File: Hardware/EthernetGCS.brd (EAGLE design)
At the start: 72.4 x 46 mm, 80 parts, among them IC1 PIC24FJ64GA002_QFN, IC3 24AA00OT, J2 HR911105A, Q2 25Mhz, U1 MIC5219-3.3V, U3 MIC5219-3.3V, U4 ENC28J60-QFN, U5 MIC5219-3.3V, U7 FT232RL-BASICSSOP, X2 USB-A-H

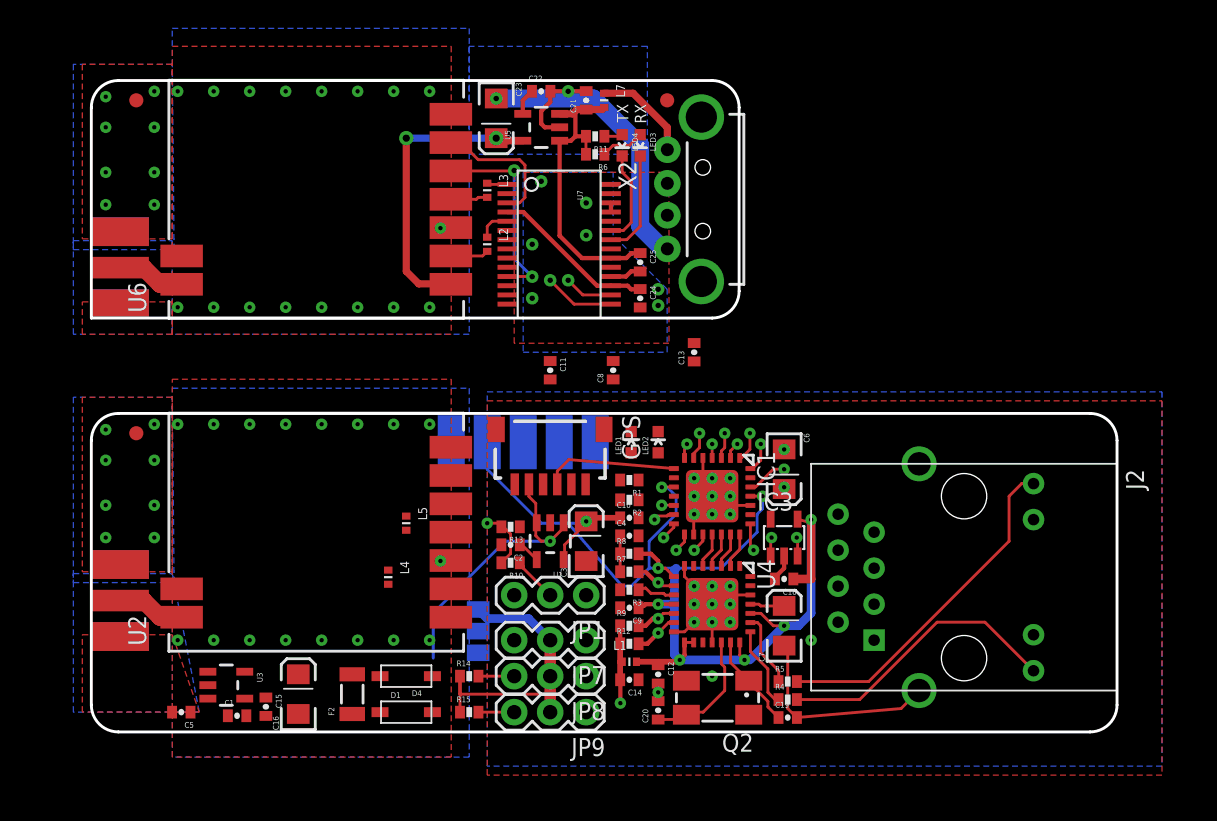
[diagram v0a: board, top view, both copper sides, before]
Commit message: More layout. Deleting reference board, adding ground planes.
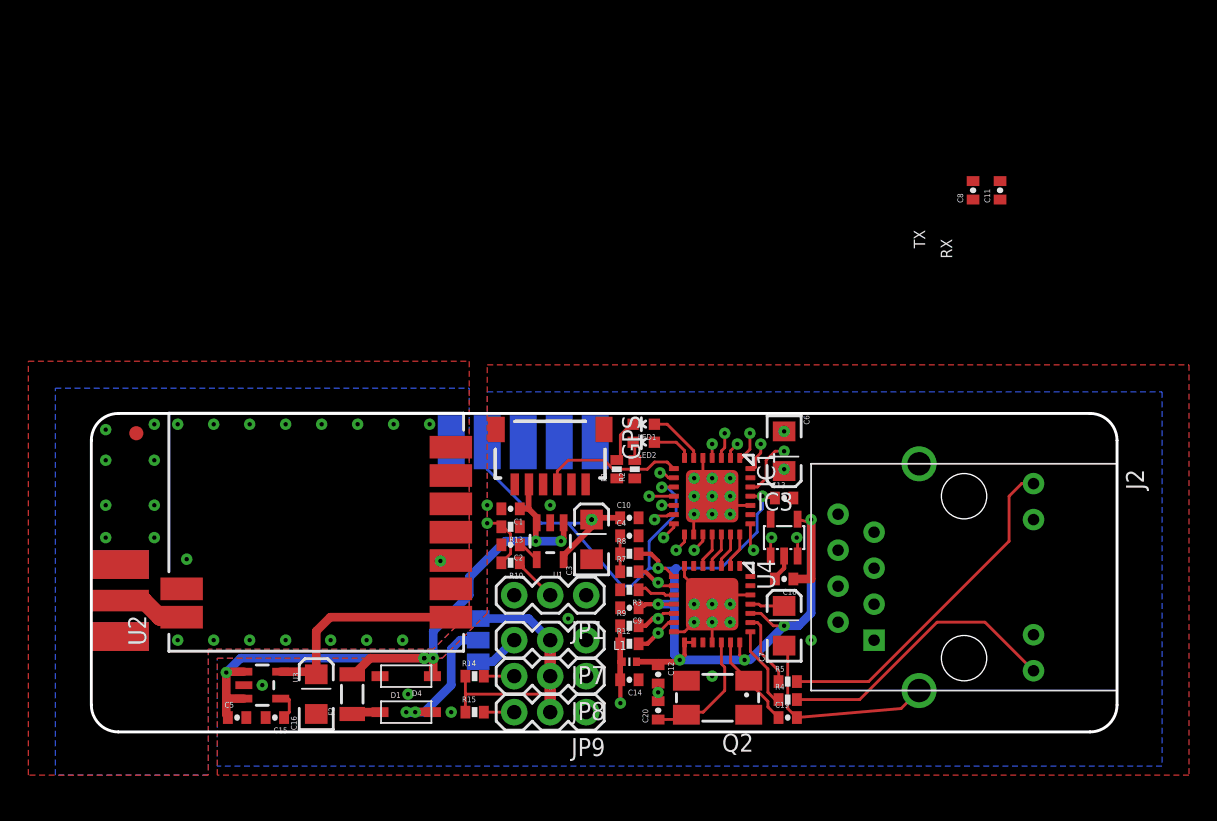
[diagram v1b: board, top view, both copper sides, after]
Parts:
- removed C21: 1uF, SparkFun:0402-CAP
- removed C22: 470pF, SparkFun:0402-CAP
- removed C23: 10uF, SparkFun:EIA3216
- removed C24, C25: 0.1uF, SparkFun:0402-CAP
- removed J$2: SMA_EDGE, 3DRobotics:SMA-EDGE
- removed JP3, JP4: FIDUCIAL1X2, SparkFun:FIDUCIAL-1X2
- removed L2, L3, L4, L5: BLM15HD102SN1, pel_dipol_comp:0402-IND
- removed L7: BKP1005HS121-T, pel_dipol_comp:0402-IND
- removed LED3: GREEN, SparkFun:LED-0603
- removed LED4: RED, SparkFun:LED-0603
- removed R11, R6: 330, SparkFun:0402-RES
- removed U5: MIC5219-3.3V, SparkFun:SOT23-5
- removed U6: (no value), 3DRobotics:HM-TRP-SMD
- removed U7: FT232RL-BASICSSOP, SparkFun:SSOP28DB
- removed X2: USB-A-H, SparkFun:USB-A-H
- moved C11 34.2 mm to (64.1, 37.5), turned to 90 degrees
- moved C8 28.4 mm to (62.2, 37.5)
- moved C1 24.2 mm to (29.6, 15.0), turned to 180 degrees
- moved C13 12.1 mm to (48.9, 15.7), turned to 0 degrees
- moved C5 3.96 mm to (10.3, 0.25), turned to 0 degrees
- moved U3 2.54 mm to (12.1, 2.54)
- moved R2 2.19 mm to (38.4, 17.8), turned to 90 degrees
- moved LED1 1.55 mm to (39.0, 21.0), turned to 90 degrees
- moved C16 1.27 mm to (15.9, 1.91)
- moved C6 1.27 mm to (48.9, 19.1)
- moved R1 1.17 mm to (37.1, 17.8), turned to 90 degrees
- moved LED2 1.02 mm to (39.0, 19.7), turned to 90 degrees
- moved C15 0.99 mm to (13.0, 0.25), turned to 180 degrees
- moved SJ1 0.63 mm to (27.3, 5.71)
- moved C3 0.40 mm to (35.3, 12.8)
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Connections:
- removed net CTS1: U6.!CONFIG, U7.11
- removed net DTR1: U7.2
- removed net N$20: C22.1, U5.4
- removed net N$21: J$2.SIG, U6.ANT
- removed net N$23: C24.1, U7.17, U7.4
- removed net N$24: U7.15, X2.D+
- removed net N$25: U7.16, X2.D-
- removed net N$26: LED4.A, R11.1
- removed net N$27: LED3.A, R6.1
- removed net N$28: LED4.C, U7.23
- removed net N$29: LED3.C, U7.22
- removed net N$30: L2.P$2, U6.DTX
- removed net N$31: L3.P$2, U6.DRX
- removed net N$32: L7.P$1, X2.VBUS
- removed net N$4: L4.P$2, U2.DTX
- removed net N$7: L5.P$2, U2.DRX
- removed net RTS1: U6.!ENABLE, U7.3
- removed net RX1: L3.P$1, U7.1
- removed net TX1: L2.P$1, U7.5
- net 3.3V: no longer C23.A, U5.5, U6.VCC
- net 5V: no longer C21.1, C25.1, L7.P$2, R11.2, R6.2, U5.1, U5.3, U7.20
- net GND: now also R1.1, R2.1; no longer C21.2, C22.2, C23.C, C24.2, C25.2, J$2.GND@0, J$2.GND@1, J$2.GND@2, J$2.GND@3, LED1.C, LED2.C, U5.2, U6.AGND, U6.GND, U7.18, U7.21, U7.25, U7.26, U7.7, X2.GND
- net LED_RX: now also LED1.A; no longer R1.2
- net LED_TX: now also LED2.A; no longer R2.2
- net N$8: now also LED1.C, R1.2; no longer LED2.A, R2.1
- net N$9: now also LED2.C, R2.2; no longer LED1.A, R1.1
- net RX: now also U2.DRX; no longer L5.P$1
- net TX: now also U2.DTX; no longer L4.P$1
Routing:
- net GND: track 64.2 -> 34.3 mm, vias 81 -> 50
- net N$25: track 16.5 -> 0.00 mm, vias 1 -> 0
- net N$24: track 16.3 -> 0.00 mm, vias 1 -> 0
- net CTS1: track 14.3 -> 0.00 mm, vias 2 -> 0
- net LED_RX: track 16.5 -> 4.06 mm, vias 1 -> 0
- net LED_TX: track 14.8 -> 2.89 mm, vias 1 -> 0
- net N$23: track 11.6 -> 0.00 mm
- net V_IN: track 0.00 -> 10.7 mm, vias 0 -> 2
- net RTS1: track 9.57 -> 0.00 mm
- net GPS2: track 0.00 -> 9.37 mm, vias 0 -> 1
- net N$29: track 7.42 -> 0.00 mm
- net N$32: track 7.03 -> 0.00 mm
- net N$28: track 6.63 -> 0.00 mm
- net 3.3V: track 21.3 -> 15.7 mm, vias 2 -> 0
- net 5V: track 42.7 -> 48.2 mm, vias 1 -> 5
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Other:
- board size 72.4 x 46 mm -> 72.4 x 22.5 mm

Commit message: Layout is finished.
Or at least is seams that way.
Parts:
- removed C11, C8: 0.1uF, SparkFun:0402-CAP
- added JP3: FIDUCIAL1X2, SparkFun:FIDUCIAL-1X2
- moved U$12 47.2 mm to (70.5, 5.71), turned to 0 degrees
- moved U$11 44.1 mm to (70.5, 8.26), turned to 0 degrees
- moved U$10 41.0 mm to (70.5, 10.8), turned to 0 degrees
- moved U$9 38.0 mm to (70.5, 13.3), turned to 0 degrees
- moved U$7 35.1 mm to (70.5, 15.9), turned to 0 degrees
- moved JP2 5.12 mm to (2.54, 15.2)
- moved C2 1.27 mm to (29.6, 11.2)
- moved R10 1.27 mm to (29.6, 12.4)
- moved SJ1 0.63 mm to (26.7, 5.71)
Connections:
- net GND: no longer C11.2, C8.2
- net V+: no longer C11.1, C8.1
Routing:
- net V+: track 93.1 -> 38.7 mm, vias 9 -> 10
- net GND: track 34.3 -> 53.9 mm, vias 50 -> 46
- net CTS: track 1.00 -> 19.7 mm, vias 1 -> 2
- net TX: track 18.1 -> 36.1 mm, vias 1 -> 2
- net PGC: track 18.5 -> 34.8 mm, vias 1 -> 3
- net PGD: track 15.0 -> 30.5 mm, vias 1 -> 2
- net RX: track 16.2 -> 28.9 mm, vias 1 -> 2
- net RTS: track 21.7 -> 29.7 mm, vias 1 -> 2
- net !MCLR: track 24.6 -> 31.3 mm, vias 1 -> 2
- net V_RC: track 19.8 -> 26.0 mm
- net N$11: track 3.17 -> 5.66 mm
- net BAT_SEN: track 26.4 -> 24.4 mm
- net GPS2: track 9.37 -> 11.0 mm, vias 1 -> 2
- net N$10: track 3.17 -> 3.81 mm
- added copper zone on layer 2, net V+

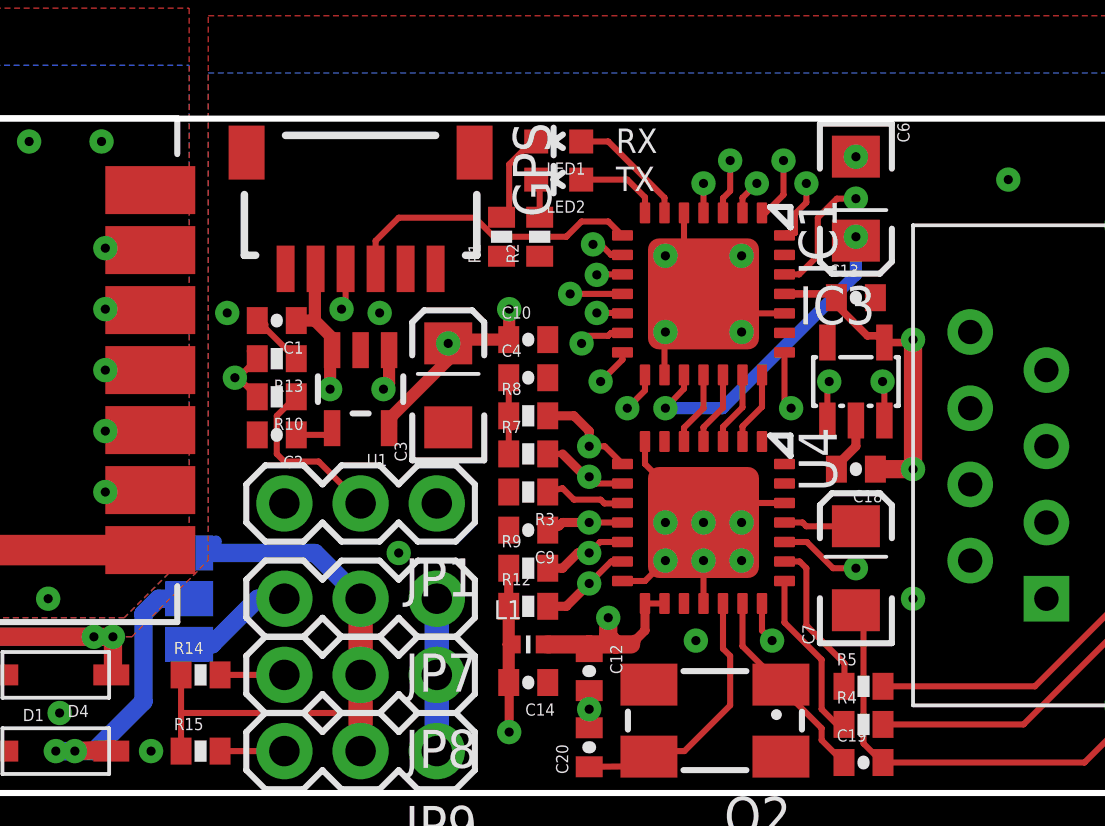
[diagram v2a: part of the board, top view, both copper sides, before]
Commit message: Organizing the schematic, small modifications to the PCB.
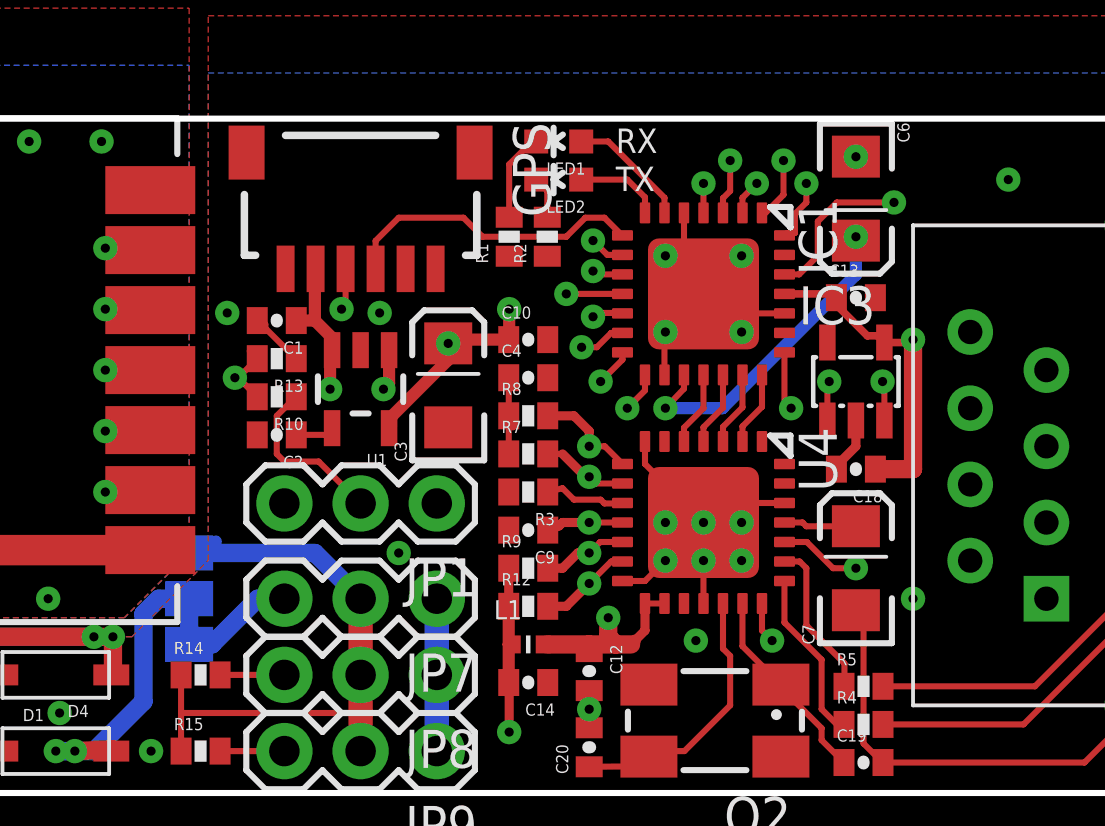
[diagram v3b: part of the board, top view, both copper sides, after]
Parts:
- IC1: value PIC24FJ64GA002_QFN -> PIC24EP128GP202_QFN
- moved R1 0.25 mm to (37.3, 17.8)
- moved R2 0.25 mm to (38.6, 17.8)
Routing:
- net V_IN: track 10.2 -> 11.5 mm
- net V+: track 38.7 -> 39.0 mm, vias 10 -> 9
